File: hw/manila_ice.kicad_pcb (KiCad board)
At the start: 4 copper layers, 85 x 54 mm, 121 parts, among them J1 USB_B, J2 RB1-125B8G1A, J3 Conn_01x08, J4 Conn_02x06_Odd_Even, J5 Conn_02x06_Odd_Even, SW1 SW_SPST, SW2 SW_SPST, SW3 SW_SPST, U1 W9812G6KH-6, U2 CH340E, U3 TPS7A7001DDA, U4 TPS7A7001DDA, U5 RTL8211EG-VB-CG, U6 ICE40HX4K-TQ144, U7 W25Q128JVS, U8 M24C01-RMN, X1 SG-7050CAN, X2 SG-7050CAN

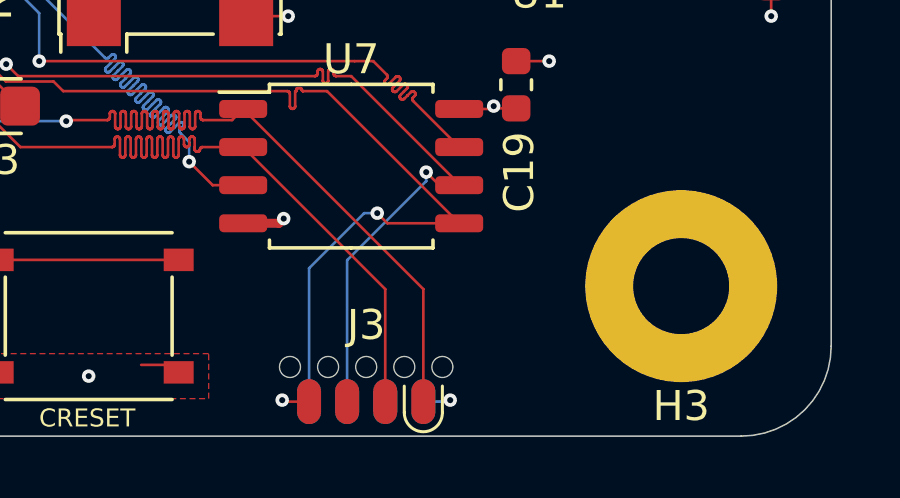
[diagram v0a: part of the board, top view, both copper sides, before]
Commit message: Add forgotten pullup to SPI flash ~CS
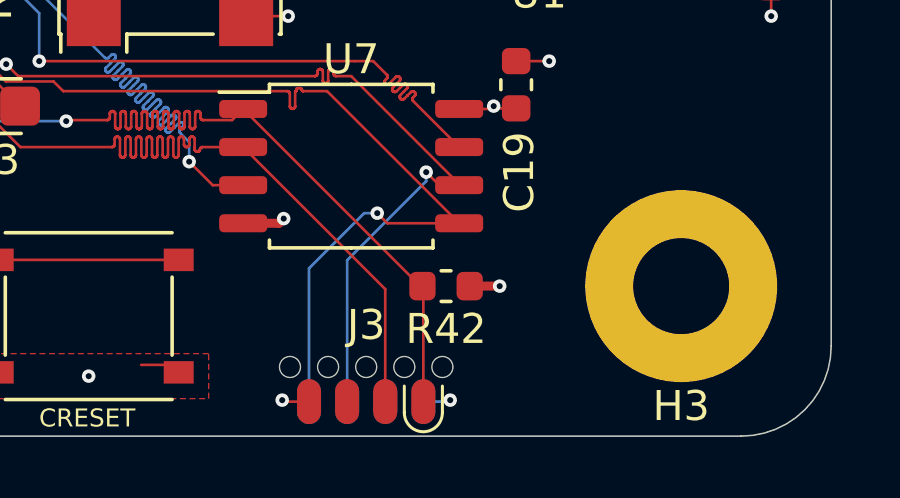
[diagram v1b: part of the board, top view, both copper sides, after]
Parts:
- added R42: 10k, Resistor_SMD:R_0603_1608Metric, F.Cu at (186.0, 119.0)
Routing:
- net +3V3: track 77.3 -> 78.3 mm, vias 52 -> 53
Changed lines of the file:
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@@
     (thickness 1.6)
     (drawings 43)
-    (tracks 21470)
+    (tracks 21472)
     (zones 0)
-    (modules 121)
+    (modules 122)
     (nets 179)
   )
   (page A4)
   (layers
-    (0 F.Cu signal hide)
+    (0 F.Cu signal)
     (1 In1.Cu signal hide)
     (2 In2.Cu signal hide)
-    (31 B.Cu signal)
+    (31 B.Cu signal hide)
     (32 B.Adhes user hide)
     (33 F.Adhes user hide)
     (34 B.Paste user hide)
     (35 F.Paste user hide)
-    (36 B.SilkS user)
-    (37 F.SilkS user hide)
+    (36 B.SilkS user hide)
+    (37 F.SilkS user)
     (38 B.Mask user hide)
     (39 F.Mask user hide)
@@
     (add_net GND)
   )
+  (module Resistor_SMD:R_0603_1608Metric (layer F.Cu)
+    (at 185.9625 119 180)
+    (descr "Resistor SMD 0603 (1608 Metric), square (rectangular) end terminal, IPC_7351 nominal, (Body size source: http://www.tortai-tech.com/upload/download/2011102023233369053.pdf), generated with kicad-footprint-generator")
+    (tags resistor)
+    (attr smd)
+    (fp_text reference R42 (at 0 -1.43) (layer F.SilkS)
+      (effects (font (size 1 1) (thickness 0.15)))
+    )
+    (fp_text value 10k (at 0 1.43) (layer F.Fab)
+      (effects (font (size 1 1) (thickness 0.15)))
+    )
+    (fp_text user %R (at 0 0) (layer F.Fab)
+      (effects (font (size 0.4 0.4) (thickness 0.06)))
+    )
+    (fp_line (start 1.48 0.73) (end -1.48 0.73) (layer F.CrtYd) (width 0.05))
+    (fp_line (start 1.48 -0.73) (end 1.48 0.73) (layer F.CrtYd) (width 0.05))
+    (fp_line (start -1.48 -0.73) (end 1.48 -0.73) (layer F.CrtYd) (width 0.05))
+    (fp_line (start -1.48 0.73) (end -1.48 -0.73) (layer F.CrtYd) (width 0.05))
+    (fp_line (start -0.162779 0.51) (end 0.162779 0.51) (layer F.SilkS) (width 0.12))
+    (fp_line (start -0.162779 -0.51) (end 0.162779 -0.51) (layer F.SilkS) (width 0.12))
+    (fp_line (start 0.8 0.4) (end -0.8 0.4) (layer F.Fab) (width 0.1))
+    (fp_line (start 0.8 -0.4) (end 0.8 0.4) (layer F.Fab) (width 0.1))
+    (fp_line (start -0.8 -0.4) (end 0.8 -0.4) (layer F.Fab) (width 0.1))
+    (fp_line (start -0.8 0.4) (end -0.8 -0.4) (layer F.Fab) (width 0.1))
+    (pad 2 smd roundrect (at 0.7875 0 180) (size 0.875 0.95) (layers F.Cu F.Paste F.Mask) (roundrect_rratio 0.25)
+      (net 33 /FPGA/~CS))
+    (pad 1 smd roundrect (at -0.7875 0 180) (size 0.875 0.95) (layers F.Cu F.Paste F.Mask) (roundrect_rratio 0.25)
+      (net 1 +3V3))
+    (model ${KISYS3DMOD}/Resistor_SMD.3dshapes/R_0603_1608Metric.wrl
+      (at (xyz 0 0 0))
+      (scale (xyz 1 1 1))
+      (rotate (xyz 0 0 0))
+    )
+  )
   (module Capacitor_SMD:C_0603_1608Metric (layer F.Cu)
     (at 171.85 89.7 90)
@@
   (segment (start 169.8825 90.4875) (end 169.875 90.495) (width 0.3) (layer F.Cu) (net 1))
   (segment (start 171.85 90.4875) (end 169.8825 90.4875) (width 0.3) (layer F.Cu) (net 1))
+  (via (at 187.75 119) (size 0.45) (drill 0.2) (layers F.Cu B.Cu) (net 1))
+  (segment (start 186.75 119) (end 187.75 119) (width 0.3) (layer F.Cu) (net 1))
   (via (at 125.5 117.5) (size 0.45) (drill 0.2) (layers F.Cu B.Cu) (net 2))
   (segment (start 124.5875 117.5) (end 125.5 117.5) (width 0.0889) (layer F.Cu) (net 2))
